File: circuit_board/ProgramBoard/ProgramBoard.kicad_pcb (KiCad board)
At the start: 4 copper layers, 25.2 x 22.6 mm, 3 parts, among them P1 CONN5X2, P2 TC2030_IDC, P3 TC2030_IDC

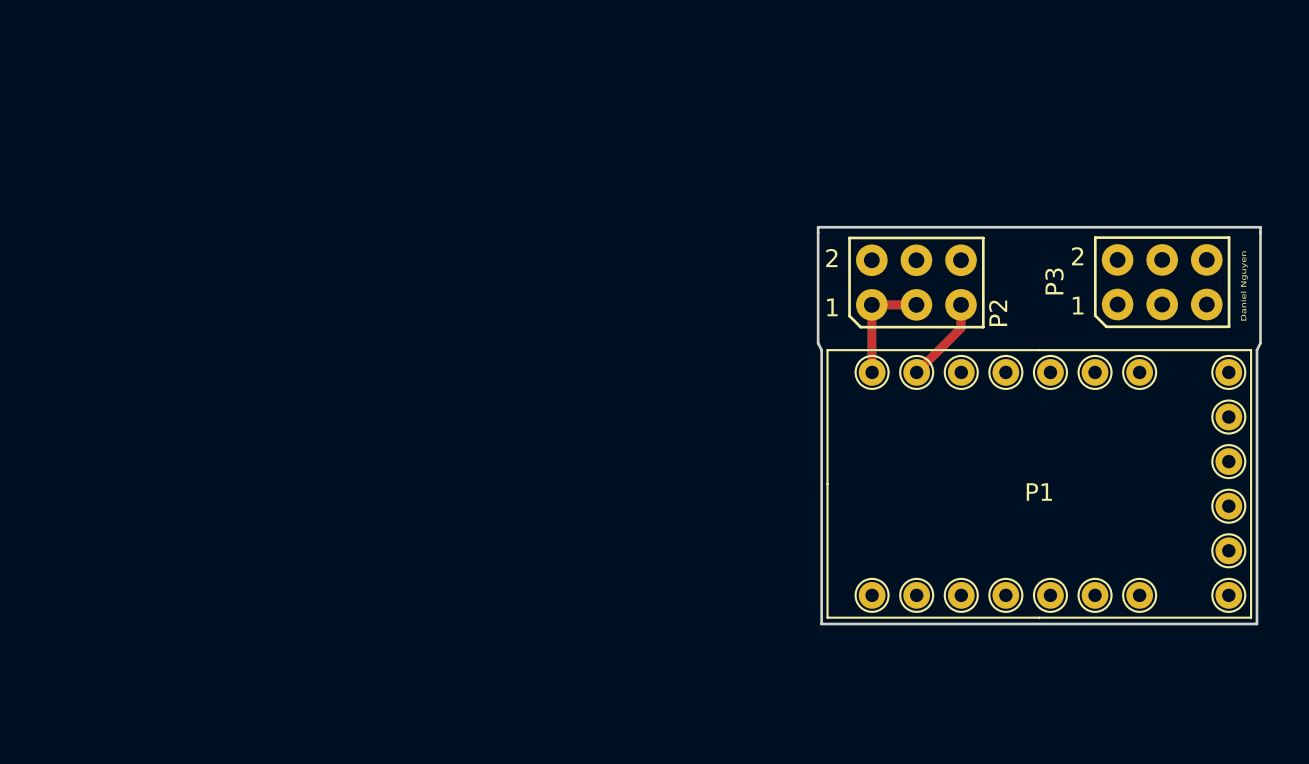
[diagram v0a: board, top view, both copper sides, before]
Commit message: examined the program board
try to switch to 10 pin tag cable to combine the programmer, UART, and power.
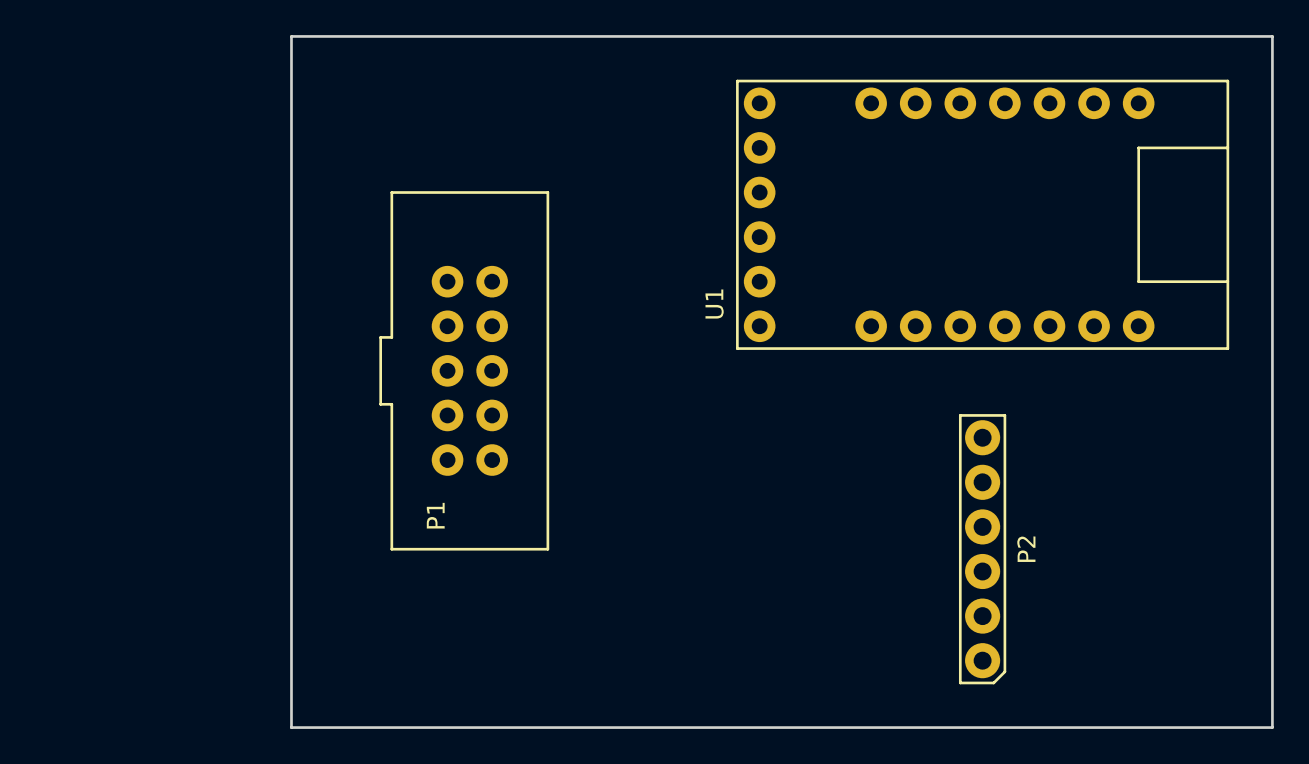
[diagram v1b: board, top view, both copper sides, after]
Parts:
- removed P3: TC2030_IDC, SensorDemo_pcb:HEADER_3X2
- added U1: SparkFun_FT231X_Breakout, SensorDemo_pcb:SparkFun_FT231X_Breakout, F.Cu at (129.5, 97.8)
- P1: footprint SensorDemo_pcb:FT231X_breakout -> SensorDemo_pcb:IDC_10
- P2: value TC2030_IDC -> HEADER_6; footprint SensorDemo_pcb:HEADER_3X2 -> SensorDemo_pcb:HEADER_6
- moved P1 32.5 mm to (99.1, 106.7), turned to 270 degrees
- moved P2 15.7 mm to (128.3, 116.8), turned to 90 degrees
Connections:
- P1 pad 1: GND -> (no net)
- P1 pad 2: +5V -> (no net)
- P2 pad 1: GND -> (no net)
- P2 pad 3: GND -> (no net)
- P2 pad 5: +5V -> (no net)
- P2 pad 6: +5V -> (no net)
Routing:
- net GND: track 6.40 -> 0.00 mm
- net +5V: track 4.95 -> 0.00 mm
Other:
- board size 25.2 x 22.6 mm -> 55.9 x 39.4 mm
- board text removed: "1"
- board text removed: "2"
- board text removed: "Daniel Nguyen"

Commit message: SensorDemo and Program board modified
1. SensorDemo board minor adjustment, 3D models added.
2. the TC2050 cable is added and routed on programmer board.
3. 3D models are added into the library.
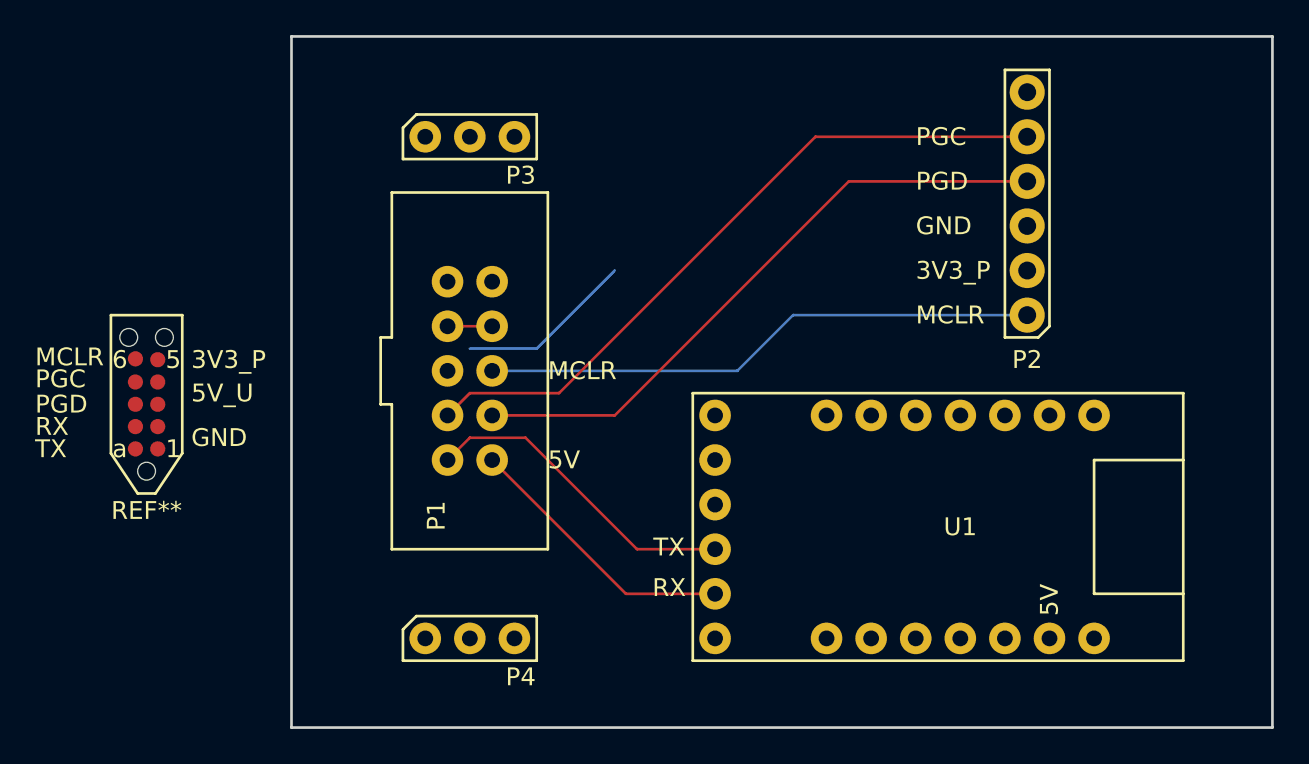
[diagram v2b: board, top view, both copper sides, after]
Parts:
- added P3: HEADER_3, SensorDemo_pcb:HEADER_3, F.Cu at (99.1, 93.3)
- added P4: HEADER_3, SensorDemo_pcb:HEADER_3, F.Cu at (99.1, 121.9)
- added REF**: TC2050, SensorDemo_pcb:TC2050, F.Cu at (80.6, 112.4)
- P1: value CONN5X2 -> IDC-10
- moved P2 19.8 mm to (130.8, 97.2)
- moved U1 18.0 mm to (127.0, 115.6)
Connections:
- P1 pad 1: (no net) -> GND
- P1 pad 10: (no net) -> Net-(P1-Pad10)
- P1 pad 2: (no net) -> GND
- P1 pad 3: (no net) -> Net-(P1-Pad3)
- P1 pad 4: (no net) -> Net-(P1-Pad3)
- P1 pad 5: (no net) -> Net-(P1-Pad5)
- P1 pad 6: (no net) -> Net-(P1-Pad6)
- P1 pad 7: (no net) -> Net-(P1-Pad7)
- P1 pad 8: (no net) -> Net-(P1-Pad8)
- P1 pad 9: (no net) -> Net-(P1-Pad9)
- P2 pad 1: (no net) -> Net-(P1-Pad6)
- P2 pad 2: (no net) -> Net-(P2-Pad2)
- P2 pad 3: (no net) -> GND
- P2 pad 4: (no net) -> Net-(P1-Pad8)
- P2 pad 5: (no net) -> Net-(P1-Pad7)
- U1 pad 11: (no net) -> Net-(P1-Pad9)
- U1 pad 12: (no net) -> Net-(P1-Pad10)
- U1 pad 20: (no net) -> +5V
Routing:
- net Net-(P1-Pad7): track 0.00 -> 39.6 mm
- net Net-(P1-Pad8): track 0.00 -> 36.0 mm
- net Net-(P1-Pad6): track 0.00 -> 31.8 mm
- net Net-(P1-Pad9): track 0.00 -> 18.4 mm
- net Net-(P1-Pad10): track 0.00 -> 15.9 mm
- net (no net): track 0.00 -> 10.1 mm
- net Net-(P1-Pad3): track 0.00 -> 2.54 mm
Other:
- board text added: "3V3_P"
- board text added: "5V"
- board text added: "5V_U"
- board text added: "GND"
- board text added: "MCLR"
- board text added: "PGC"
- board text added: "PGD"
- board text added: "RX"
- board text added: "TX"

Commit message: updated SensoDemo and ProgramBoard
INA126 is replaced by INA333.
TC2050-IDC-NL cable will be used for powering and programming.
both boards should be done.
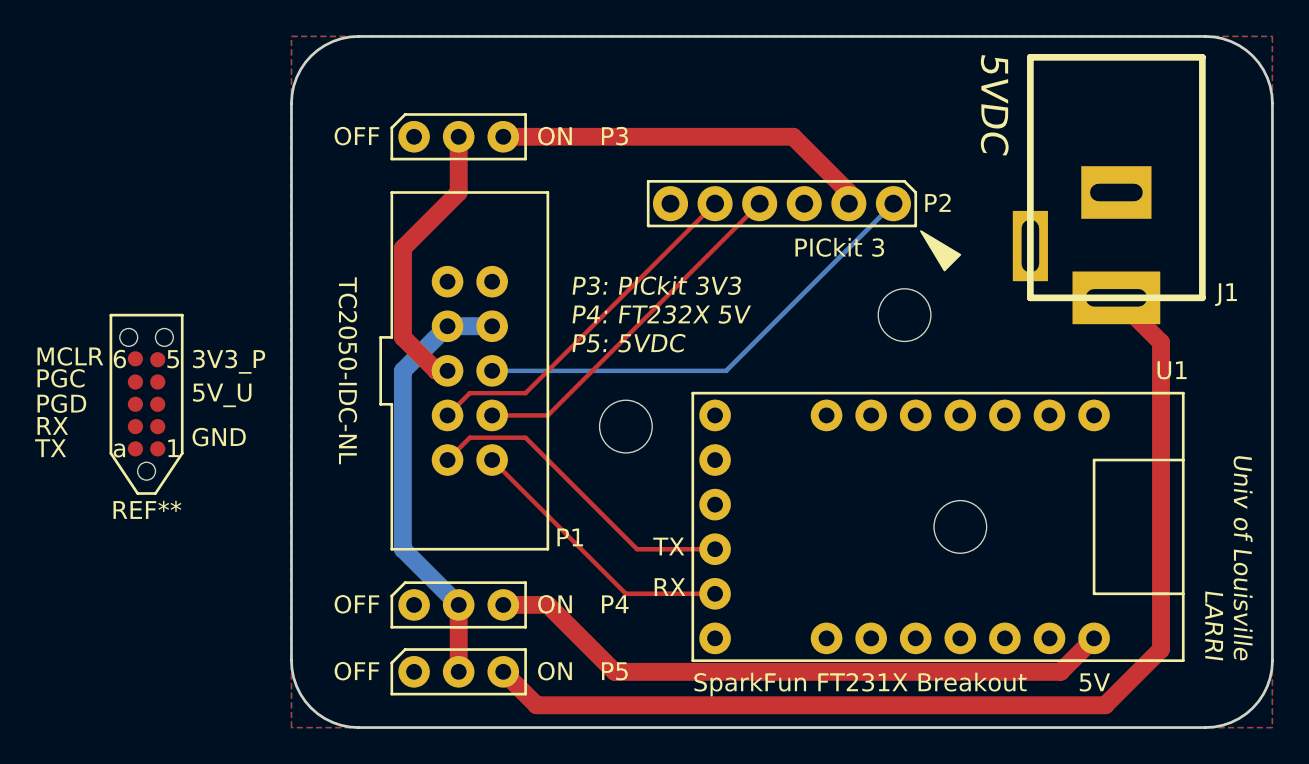
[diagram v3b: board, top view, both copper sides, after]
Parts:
- added G***: LOGO, Global_PCB_Library:logo_RZ_short, B.Cu at (107.3, 123.8)
- added J1: BARREL_JACK, SensorDemo_pcb:BARREL_JACK, F.Cu at (135.9, 96.5)
- added MH3: MH, SensorDemo_pcb:MH_3MM, F.Cu at (108.0, 109.9)
- added MH3: MH, SensorDemo_pcb:MH_3MM, F.Cu at (127.0, 115.6)
- added MH3: MH, SensorDemo_pcb:MH_3MM, F.Cu at (123.8, 103.5)
- added P5: HEADER_3, SensorDemo_pcb:HEADER_3, F.Cu at (98.4, 123.8)
- moved P2 14.0 mm to (116.8, 97.2), turned to 180 degrees
- moved P4 2.01 mm to (98.4, 120.0)
- moved P3 0.64 mm to (98.4, 93.3)
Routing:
- net Net-(J1-Pad1): track 0.00 -> 60.7 mm
- net +5V: track 0.00 -> 36.0 mm
- net Net-(P1-Pad3): track 2.54 -> 24.6 mm
- net Net-(P2-Pad2): track 0.00 -> 21.6 mm
- net Net-(P1-Pad7): track 39.6 -> 20.2 mm
- net Net-(P1-Pad5): track 0.00 -> 16.1 mm
- net Net-(P1-Pad8): track 36.0 -> 20.2 mm
- net (no net): track 10.1 -> 0.00 mm
- net Net-(P1-Pad6): track 31.8 -> 26.8 mm
- added copper zone on B.Cu, net GND
- added copper zone on F.Cu, net GND
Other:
- outline, holes or cut-outs redrawn
- copper layers 4 -> 2
- board text added: "5VDC"
- board text added: "OFF"
- board text added: "ON"
- board text added: "P3: PICkit 3V3 P4: FT232X 5V P5: 5VDC"
- board text added: "PICkit 3"
- board text added: "SparkFun FT231X Breakout"
- board text added: "TC2050-IDC-NL"
- board text added: "Univ of Louisville LARRI"

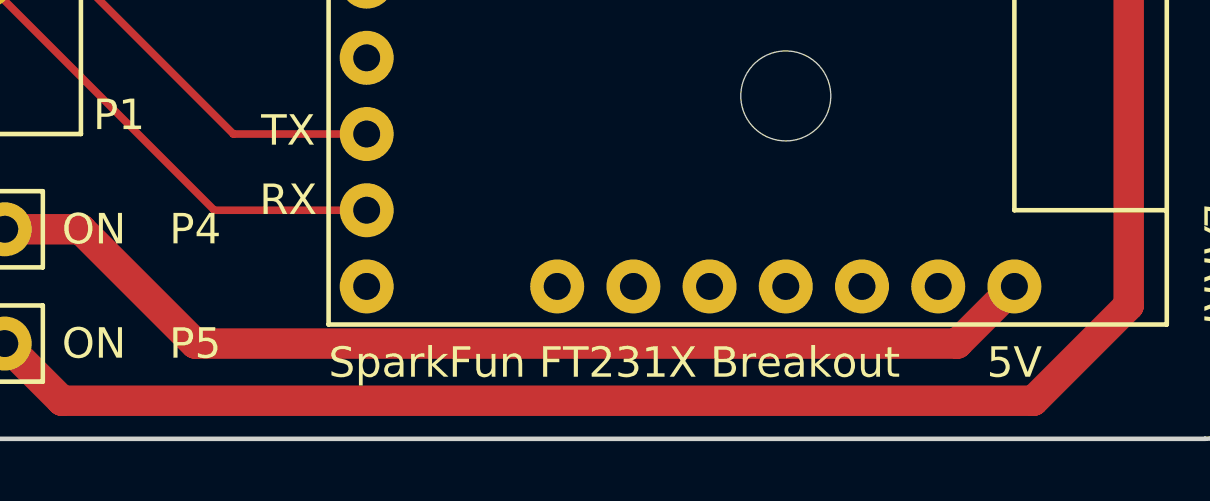
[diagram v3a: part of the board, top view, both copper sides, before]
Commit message: updated schematic
-fixed programming board 5v
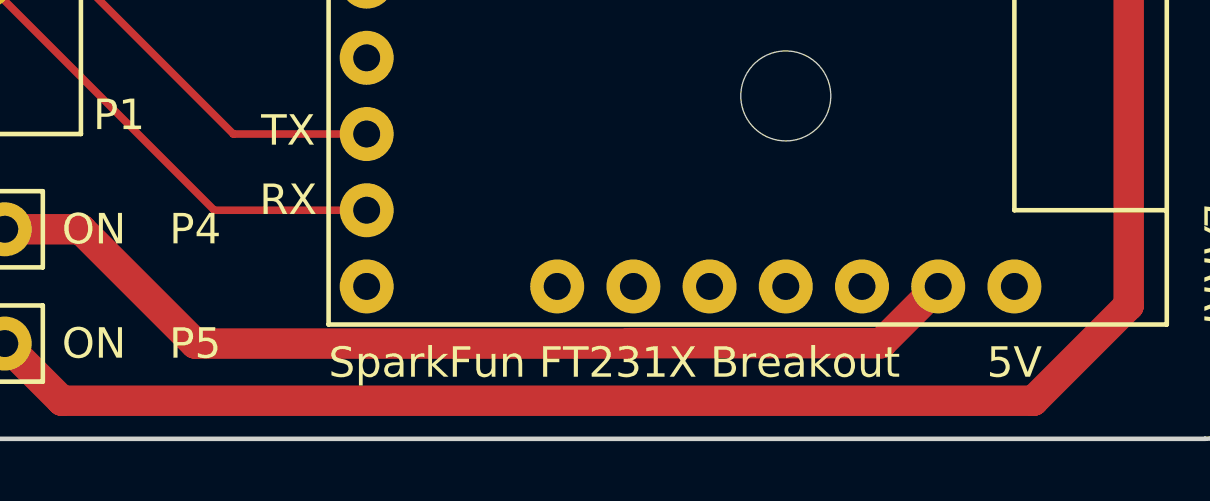
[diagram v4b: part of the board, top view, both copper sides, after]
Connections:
- J1 pad 2: (no net) -> Net-(J1-Pad2)
- P2 pad 6: (no net) -> Net-(P2-Pad6)
- P3 pad 1: (no net) -> Net-(P3-Pad1)
- P4 pad 1: (no net) -> Net-(P4-Pad1)
- P5 pad 1: (no net) -> Net-(P5-Pad1)
- U1 pad 1: (no net) -> Net-(U1-Pad1)
- U1 pad 10: (no net) -> Net-(U1-Pad10)
- U1 pad 13: (no net) -> Net-(U1-Pad13)
- U1 pad 14: (no net) -> Net-(U1-Pad14)
- U1 pad 15: (no net) -> Net-(U1-Pad15)
- U1 pad 16: (no net) -> Net-(U1-Pad16)
- U1 pad 17: (no net) -> Net-(U1-Pad17)
- U1 pad 18: (no net) -> Net-(U1-Pad18)
- U1 pad 19: (no net) -> +5V
- U1 pad 2: (no net) -> Net-(U1-Pad2)
- U1 pad 20: +5V -> Net-(U1-Pad20)
- U1 pad 3: (no net) -> Net-(U1-Pad3)
- U1 pad 4: (no net) -> Net-(U1-Pad4)
- U1 pad 5: (no net) -> Net-(U1-Pad5)
- U1 pad 6: (no net) -> Net-(U1-Pad6)
- U1 pad 7: (no net) -> Net-(U1-Pad7)
- U1 pad 8: (no net) -> Net-(U1-Pad8)
- U1 pad 9: (no net) -> Net-(U1-Pad9)
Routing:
- net +5V: track 36.0 -> 33.5 mm

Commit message: Revert "Revert "Merge branch 'master' of https://github.com/zrs5532/mri_demo""
This reverts commit c7bcd66b67d9c03c78e75f611b5453059c538dec.
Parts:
- removed REF**: TC2050, SensorDemo_pcb:TC2050
- moved G*** 32.6 mm to (108.8, 91.2)
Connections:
- J1 pad 2: Net-(J1-Pad2) -> GND
- J1 pad 3: GND -> (no net)
- P2 pad 6: Net-(P2-Pad6) -> (no net)
- P3 pad 1: Net-(P3-Pad1) -> (no net)
- P4 pad 1: Net-(P4-Pad1) -> (no net)
- P5 pad 1: Net-(P5-Pad1) -> (no net)
- U1 pad 1: Net-(U1-Pad1) -> (no net)
- U1 pad 10: Net-(U1-Pad10) -> (no net)
- U1 pad 13: Net-(U1-Pad13) -> (no net)
- U1 pad 14: Net-(U1-Pad14) -> (no net)
- U1 pad 15: Net-(U1-Pad15) -> (no net)
- U1 pad 16: Net-(U1-Pad16) -> (no net)
- U1 pad 17: Net-(U1-Pad17) -> (no net)
- U1 pad 18: Net-(U1-Pad18) -> (no net)
- U1 pad 2: Net-(U1-Pad2) -> (no net)
- U1 pad 20: Net-(U1-Pad20) -> GND
- U1 pad 3: Net-(U1-Pad3) -> (no net)
- U1 pad 4: Net-(U1-Pad4) -> (no net)
- U1 pad 5: Net-(U1-Pad5) -> (no net)
- U1 pad 6: Net-(U1-Pad6) -> (no net)
- U1 pad 7: Net-(U1-Pad7) -> (no net)
- U1 pad 8: Net-(U1-Pad8) -> GND
- U1 pad 9: Net-(U1-Pad9) -> (no net)
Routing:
- net Net-(J1-Pad1): track 60.7 -> 58.8 mm
- removed copper zone on F.Cu, net GND
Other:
- board text added: "Daniel &"
- board text added: "MRI P'n'P Sensor Demo Supply Univ of Louisville - LARRI"
- board text removed: "3V3_P"
- board text removed: "5V_U"
- board text removed: "GND"
- board text removed: "MCLR"
- board text removed: "PGC"
- board text removed: "PGD"
- board text removed: "RX"
- board text removed: "TX"
- board text removed: "Univ of Louisville LARRI"

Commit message: Revert "Merge branch 'master' of https://github.com/zrs5532/mri_demo"
This reverts commit b0c8028f714b16f114d60085c0a86ac2043fc740, reversing
changes made to 0fccd9f34ae5c363ed48057d6b873a7540cc24aa.
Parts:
- added REF**: TC2050, SensorDemo_pcb:TC2050, F.Cu at (80.6, 112.4)
- moved G*** 32.6 mm to (107.3, 123.8)
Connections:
- J1 pad 2: GND -> Net-(J1-Pad2)
- J1 pad 3: (no net) -> GND
- P2 pad 6: (no net) -> Net-(P2-Pad6)
- P3 pad 1: (no net) -> Net-(P3-Pad1)
- P4 pad 1: (no net) -> Net-(P4-Pad1)
- P5 pad 1: (no net) -> Net-(P5-Pad1)
- U1 pad 1: (no net) -> Net-(U1-Pad1)
- U1 pad 10: (no net) -> Net-(U1-Pad10)
- U1 pad 13: (no net) -> Net-(U1-Pad13)
- U1 pad 14: (no net) -> Net-(U1-Pad14)
- U1 pad 15: (no net) -> Net-(U1-Pad15)
- U1 pad 16: (no net) -> Net-(U1-Pad16)
- U1 pad 17: (no net) -> Net-(U1-Pad17)
- U1 pad 18: (no net) -> Net-(U1-Pad18)
- U1 pad 2: (no net) -> Net-(U1-Pad2)
- U1 pad 20: GND -> Net-(U1-Pad20)
- U1 pad 3: (no net) -> Net-(U1-Pad3)
- U1 pad 4: (no net) -> Net-(U1-Pad4)
- U1 pad 5: (no net) -> Net-(U1-Pad5)
- U1 pad 6: (no net) -> Net-(U1-Pad6)
- U1 pad 7: (no net) -> Net-(U1-Pad7)
- U1 pad 8: GND -> Net-(U1-Pad8)
- U1 pad 9: (no net) -> Net-(U1-Pad9)
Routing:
- net Net-(J1-Pad1): track 58.8 -> 60.7 mm
- added copper zone on F.Cu, net GND
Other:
- board text added: "3V3_P"
- board text added: "5V_U"
- board text added: "GND"
- board text added: "MCLR"
- board text added: "PGC"
- board text added: "PGD"
- board text added: "RX"
- board text added: "TX"
- board text added: "Univ of Louisville LARRI"
- board text removed: "Daniel &"
- board text removed: "MRI P'n'P Sensor Demo Supply Univ of Louisville - LARRI"
